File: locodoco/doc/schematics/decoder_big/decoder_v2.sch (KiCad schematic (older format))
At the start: 80 parts, among them IC1 IRF8313, IC2 ATMega8/48/88/168/328, P1 CONN_5, P11 CONN_1, P12 CONN_1, P13 CONN_1, P16 CONN_1, P17 CONN_1, P2 CONN_2, P20 CONN_1, P22 CONN_1, P23 CONN_1, P24 CONN_2, P25 CONN_2, P3 CONN_1, P4 CONN_1, P5 CONN_1, P6 CONN_1, P7 CONN_1, P8 CONN_1, U1 L6201PS, U2 ULN2003A, U5 RFM12, U6 LM257X, X1 QUARTZCMS4

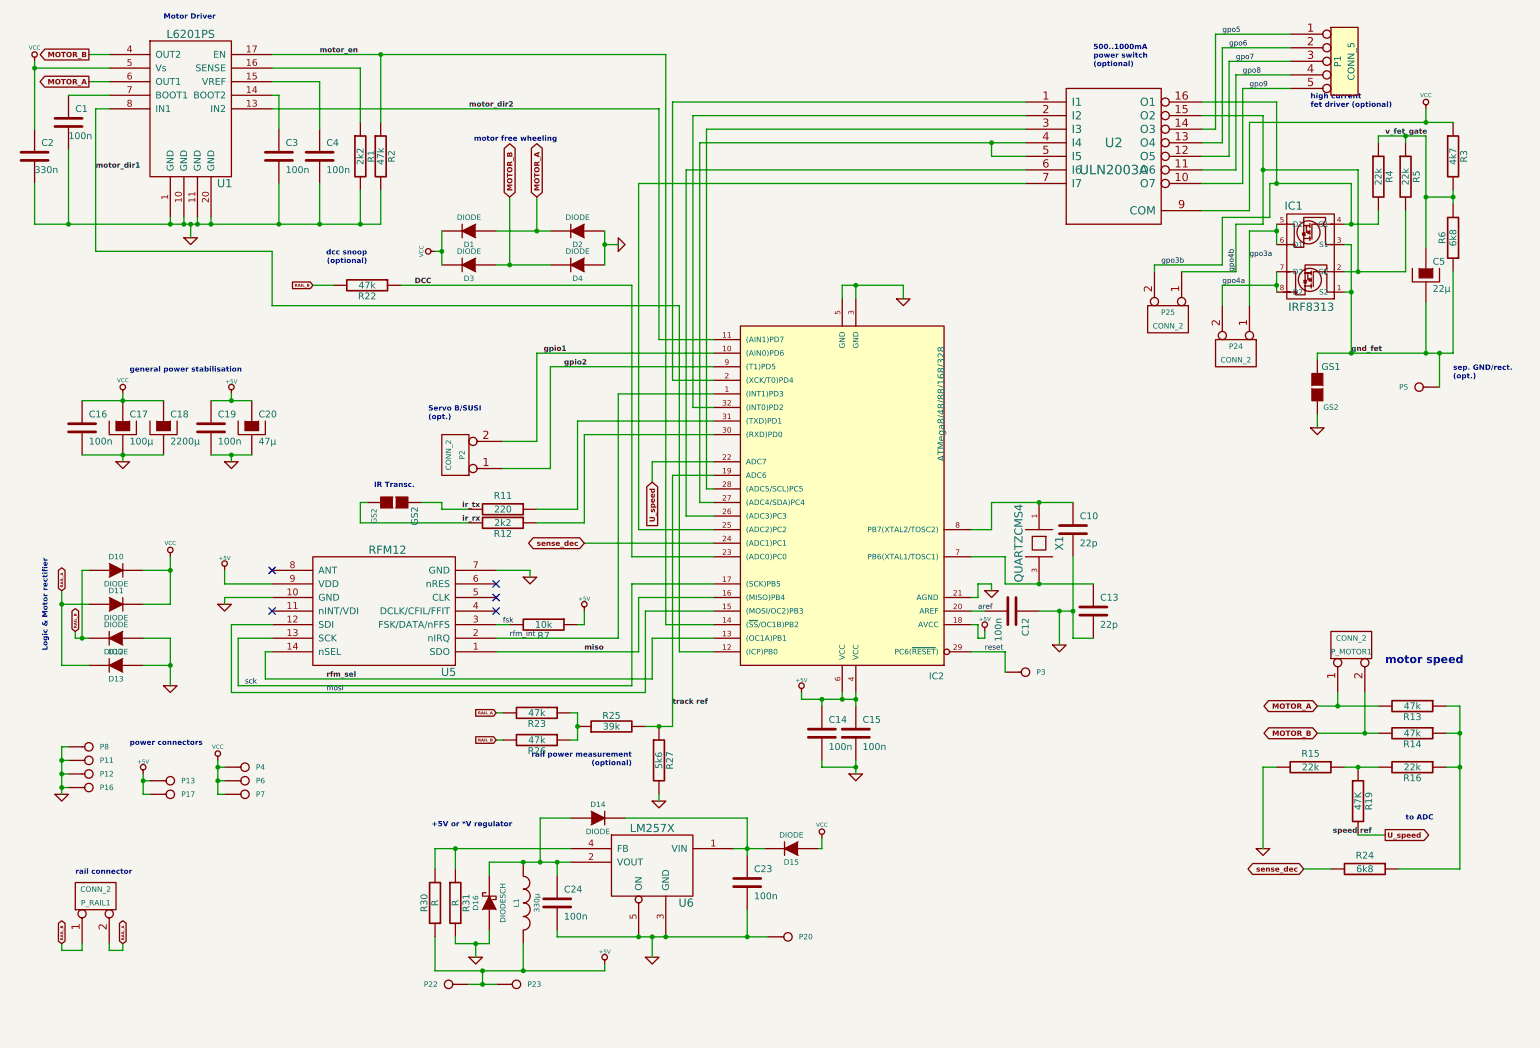
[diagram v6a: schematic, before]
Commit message: motor speed measurement: impedance of circuit adjusted
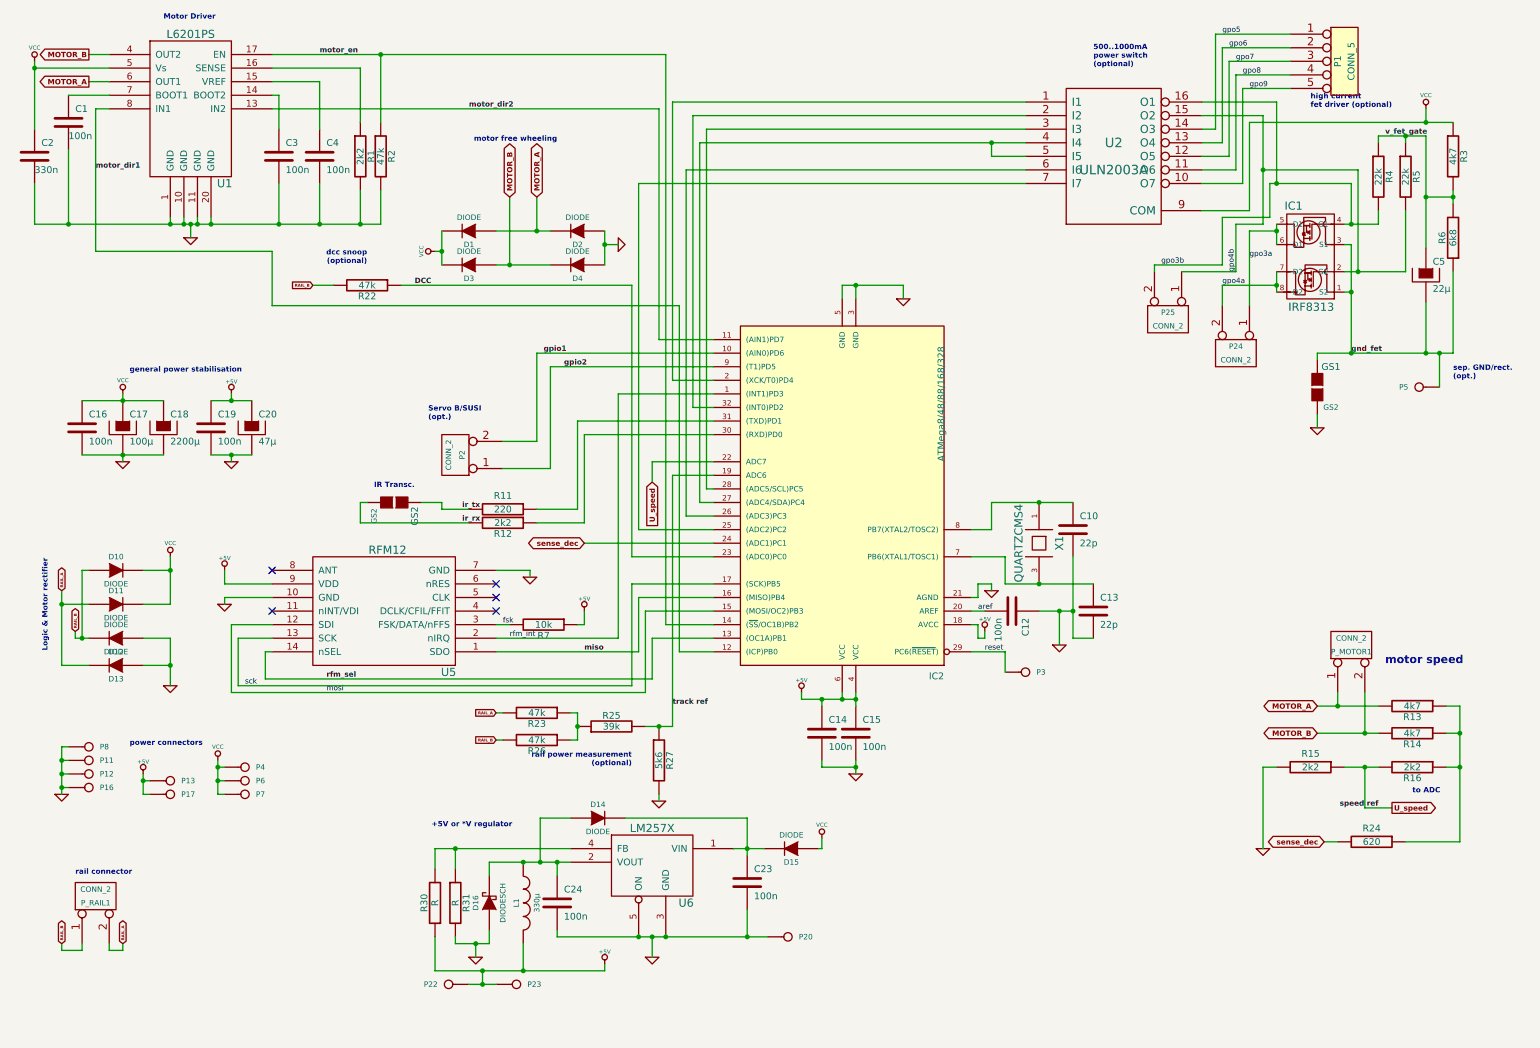
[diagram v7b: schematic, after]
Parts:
- removed R19: 47K, symbol R
- R13, R14: value 47k -> 4k7
- R15, R16: value 22k -> 2k2
- R24: value 6k8 -> 620
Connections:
- net U_speed: now also R15.1, R16.2
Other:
- moved on the sheet: R24
